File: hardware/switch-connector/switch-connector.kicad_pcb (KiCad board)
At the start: 2 copper layers, 10 parts, among them P1 12V, P2 Relay OFF (NC), P3 Sensing, P4 Coil, P5 Relay On enable (NO), P6 NO, P7 Common, SW1 NC: Off, SW2 NO: On, SW3 NC: Emergency Off

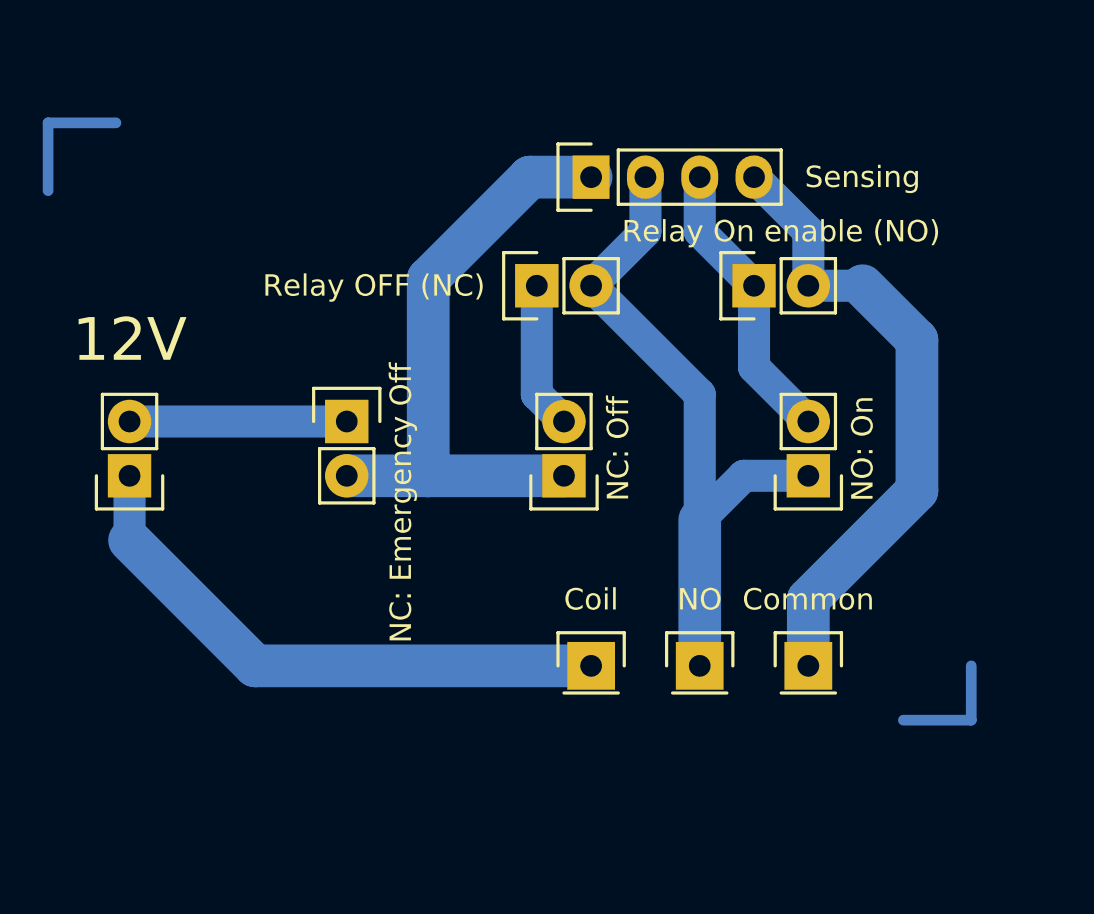
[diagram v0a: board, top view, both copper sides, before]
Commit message: o Update board with new connectors.
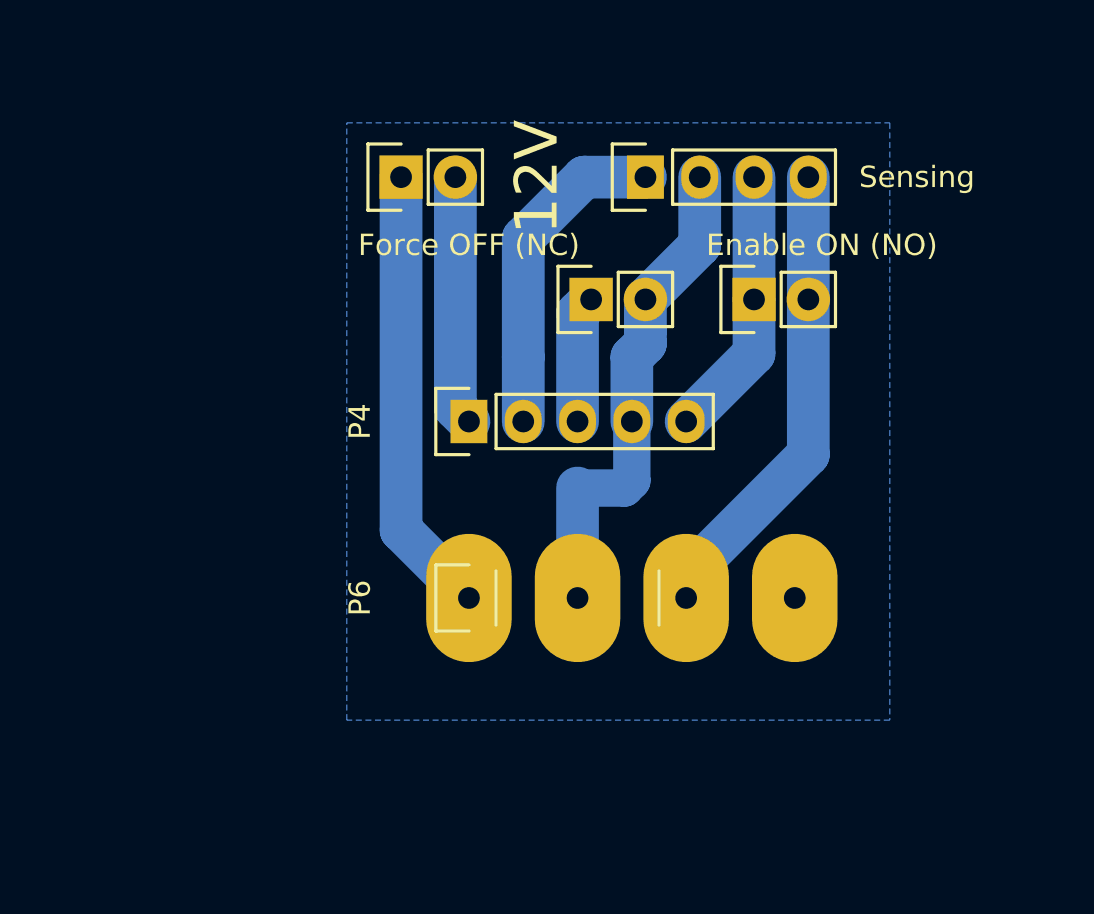
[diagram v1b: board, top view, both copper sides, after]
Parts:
- removed P7: Common, Pin_Headers:Pin_Header_Straight_1x01
- removed SW1: NC: Off, Pin_Headers:Pin_Header_Straight_1x02
- removed SW2: NO: On, Pin_Headers:Pin_Header_Straight_1x02
- removed SW3: NC: Emergency Off, Pin_Headers:Pin_Header_Straight_1x02
- P2: value Relay OFF (NC) -> Force OFF (NC)
- P4: value Coil -> SwitchConnector; footprint Pin_Headers:Pin_Header_Straight_1x01 -> Pin_Headers:Pin_Header_Straight_1x05
- P5: value Relay On enable (NO) -> Enable ON (NO)
- P6: value NO -> HV-RelayConnector; footprint Pin_Headers:Pin_Header_Straight_1x01 -> Pin_Headers:Pin_Header_Straight_1x04
- moved P1 18.9 mm to (168.9, 100.3), turned to 90 degrees
- moved P4 12.8 mm to (172.1, 111.8), turned to 90 degrees
- moved P6 11.3 mm to (172.1, 120.0), turned to 90 degrees
- moved P2 2.62 mm to (177.8, 106.0)
- moved P3 2.54 mm to (180.3, 100.3)
- moved P5 0.64 mm to (185.4, 106.0)
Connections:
- P1 pad 1: Net-(P1-Pad1) -> GND
- P1 pad 2: Net-(P1-Pad2) -> +12V
- P2 pad 2: Net-(P2-Pad2) -> /switch-box/Sense-Off
- P3 pad 1: Net-(P3-Pad1) -> /switch-box/Sense-E-Stop
- P3 pad 2: Net-(P2-Pad2) -> /switch-box/Sense-Off
- P3 pad 3: Net-(P3-Pad3) -> /switch-box/Sense-On
- P3 pad 4: Net-(P3-Pad4) -> /switch-box/Sense-Powered
- P4 pad 1: Net-(P1-Pad1) -> +12V
- P5 pad 1: Net-(P3-Pad3) -> /switch-box/Sense-On
- P5 pad 2: Net-(P3-Pad4) -> /switch-box/Sense-Powered
- P6 pad 1: Net-(P2-Pad2) -> GND
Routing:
- net Net-(P2-Pad2): track 32.0 -> 0.00 mm
- net Net-(P3-Pad4): track 29.6 -> 0.00 mm
- net Net-(P3-Pad1): track 29.0 -> 0.00 mm
- net Net-(P1-Pad1): track 27.0 -> 0.00 mm
- net /switch-box/Sense-Off: track 0.00 -> 26.1 mm
- net /switch-box/Sense-Powered: track 0.00 -> 22.1 mm
- net GND: track 0.00 -> 21.0 mm
- net /switch-box/Sense-E-Stop: track 0.00 -> 15.5 mm
- net Net-(P3-Pad3): track 13.5 -> 0.00 mm
- net /switch-box/Sense-On: track 0.00 -> 12.7 mm
- net (no net): track 12.1 -> 0.00 mm
- net +12V: track 0.00 -> 11.7 mm
- net Net-(P1-Pad2): track 10.2 -> 0.00 mm
- net Net-(P2-Pad1): track 6.88 -> 5.97 mm
- added copper zone on B.Cu, net GND
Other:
- net class Default: clearance 0.2 -> 0.25
- rule trace_clearance: 0.2 -> 0.25

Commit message: o tweaks.
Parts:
- added REF**: M, Mounting_Holes:MountingHole_3.2mm_M3, F.Cu at (194.0, 122.0)
- added REF**: M, Mounting_Holes:MountingHole_3.2mm_M3, F.Cu at (194.0, 102.0)
- added REF**: M, Mounting_Holes:MountingHole_3.2mm_M3, F.Cu at (163.0, 102.0)
- added REF**: M, Mounting_Holes:MountingHole_3.2mm_M3, F.Cu at (163.0, 122.0)
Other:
- board outline added: 40 x 27.9 mm
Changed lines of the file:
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@@
     (links 11)
     (no_connects 0)
-    (area 0 0 0 0)
+    (area 157.899999 96.7925 198.100001 125.830001)
     (thickness 1.6)
     (drawings 4)
     (tracks 28)
     (zones 0)
-    (modules 6)
+    (modules 10)
     (nets 8)
   )
@@
   )
   (setup
-    (last_trace_width 2)
+    (last_trace_width 1.5)
     (user_trace_width 1.5)
     (user_trace_width 1.75)
@@
     (trace_min 0.2)
     (segment_width 0.2)
-    (edge_width 0.15)
+    (edge_width 0.2)
     (via_size 0.6)
     (via_drill 0.4)
@@
     (mod_text_size 1 1)
     (mod_text_width 0.15)
-    (pad_size 1.524 1.524)
-    (pad_drill 0.762)
+    (pad_size 3.2 3.2)
+    (pad_drill 3.2)
     (pad_to_mask_clearance 0.2)
     (aux_axis_origin 0 0)
     (visible_elements FFFFEF7F)
     (pcbplotparams
-      (layerselection 0x00020_80000000)
+      (layerselection 0x00000_fffffffe)
       (usegerberextensions false)
       (excludeedgelayer true)
@@
     (diff_pair_width 0.2)
   )
+  (module Mounting_Holes:MountingHole_3.2mm_M3 locked (layer F.Cu)
+    (at 194 122)
+    (descr "Mounting Hole 3.2mm, no annular, M3")
+    (tags "mounting hole 3.2mm no annular m3")
+    (fp_text reference REF** (at 0 -4.2) (layer F.SilkS)
+      (effects (font (size 1 1) (thickness 0.15)))
+    )
+    (fp_text value M (at 0 0) (layer F.Fab)
+      (effects (font (size 1 1) (thickness 0.15)))
+    )
+    (fp_circle (center 0 0) (end 3.2 0) (layer Cmts.User) (width 0.15))
+    (fp_circle (center 0 0) (end 3.45 0) (layer F.CrtYd) (width 0.05))
+    (pad 1 np_thru_hole circle (at 0 0) (size 3.2 3.2) (drill 3.2) (layers *.Cu *.Mask F.SilkS))
+  )
+  (module Mounting_Holes:MountingHole_3.2mm_M3 locked (layer F.Cu)
+    (at 194 102)
+    (descr "Mounting Hole 3.2mm, no annular, M3")
+    (tags "mounting hole 3.2mm no annular m3")
+    (fp_text reference REF** (at 0 -4.2) (layer F.SilkS)
+      (effects (font (size 1 1) (thickness 0.15)))
+    )
+    (fp_text value M (at 0 0 180) (layer F.Fab)
+      (effects (font (size 1 1) (thickness 0.15)))
+    )
+    (fp_circle (center 0 0) (end 3.45 0) (layer F.CrtYd) (width 0.05))
+    (fp_circle (center 0 0) (end 3.2 0) (layer Cmts.User) (width 0.15))
+    (pad 1 np_thru_hole circle (at 0 0) (size 3.2 3.2) (drill 3.2) (layers *.Cu *.Mask F.SilkS))
+  )
+  (module Mounting_Holes:MountingHole_3.2mm_M3 locked (layer F.Cu)
+    (at 163 102)
+    (descr "Mounting Hole 3.2mm, no annular, M3")
+    (tags "mounting hole 3.2mm no annular m3")
+    (fp_text reference REF** (at 0 -4.2) (layer F.SilkS)
+      (effects (font (size 1 1) (thickness 0.15)))
+    )
+    (fp_text value M (at 0 0) (layer F.Fab)
+      (effects (font (size 1 1) (thickness 0.15)))
+    )
+    (fp_circle (center 0 0) (end 3.2 0) (layer Cmts.User) (width 0.15))
+    (fp_circle (center 0 0) (end 3.45 0) (layer F.CrtYd) (width 0.05))
+    (pad 1 np_thru_hole circle (at 0 0) (size 3.2 3.2) (drill 3.2) (layers *.Cu *.Mask F.SilkS))
+  )
+  (module Mounting_Holes:MountingHole_3.2mm_M3 locked (layer F.Cu)
+    (at 163 122)
+    (descr "Mounting Hole 3.2mm, no annular, M3")
+    (tags "mounting hole 3.2mm no annular m3")
+    (fp_text reference REF** (at 0 -4.2) (layer F.SilkS)
+      (effects (font (size 1 1) (thickness 0.15)))
+    )
+    (fp_text value M (at 0 0) (layer F.Fab)
+      (effects (font (size 1 1) (thickness 0.15)))
+    )
+    (fp_circle (center 0 0) (end 3.45 0) (layer F.CrtYd) (width 0.05))
+    (fp_circle (center 0 0) (end 3.2 0) (layer Cmts.User) (width 0.15))
+    (pad 1 np_thru_hole circle (at 0 0) (size 3.2 3.2) (drill 3.2) (layers *.Cu *.Mask F.SilkS))
+  )
   (module Pin_Headers:Pin_Header_Straight_1x04 (layer F.Cu)
     (at 172.085 120.015 90)
@@
     )
   )
-  (gr_line (start 166.37 125.73) (end 166.37 97.79) (layer Margin) (width 0.2))
-  (gr_line (start 191.77 125.73) (end 166.37 125.73) (layer Margin) (width 0.2))
-  (gr_line (start 191.77 97.79) (end 191.77 125.73) (layer Margin) (width 0.2))
-  (gr_line (start 166.37 97.79) (end 191.77 97.79) (layer Margin) (width 0.2))
+  (gr_line (start 158 125.73) (end 158 97.79) (layer Edge.Cuts) (width 0.2))
+  (gr_line (start 198 125.73) (end 158 125.73) (layer Edge.Cuts) (width 0.2))
+  (gr_line (start 198 97.79) (end 198 125.73) (layer Edge.Cuts) (width 0.2))
+  (gr_line (start 158 97.79) (end 198 97.79) (layer Edge.Cuts) (width 0.2))
   (segment (start 177.8 106.05) (end 177.165 106.685) (width 2) (layer B.Cu) (net 1))
   (segment (start 177.165 106.685) (end 177.165 111.76) (width 2) (layer B.Cu) (net 1))
@@
     (polygon
       (pts
-        (xy 166.37 97.79) (xy 191.77 97.79) (xy 191.77 125.73) (xy 166.37 125.73)
+        (xy 158.75 97.79) (xy 197.485 97.79) (xy 197.485 125.73) (xy 158.75 125.73)
       )
     )

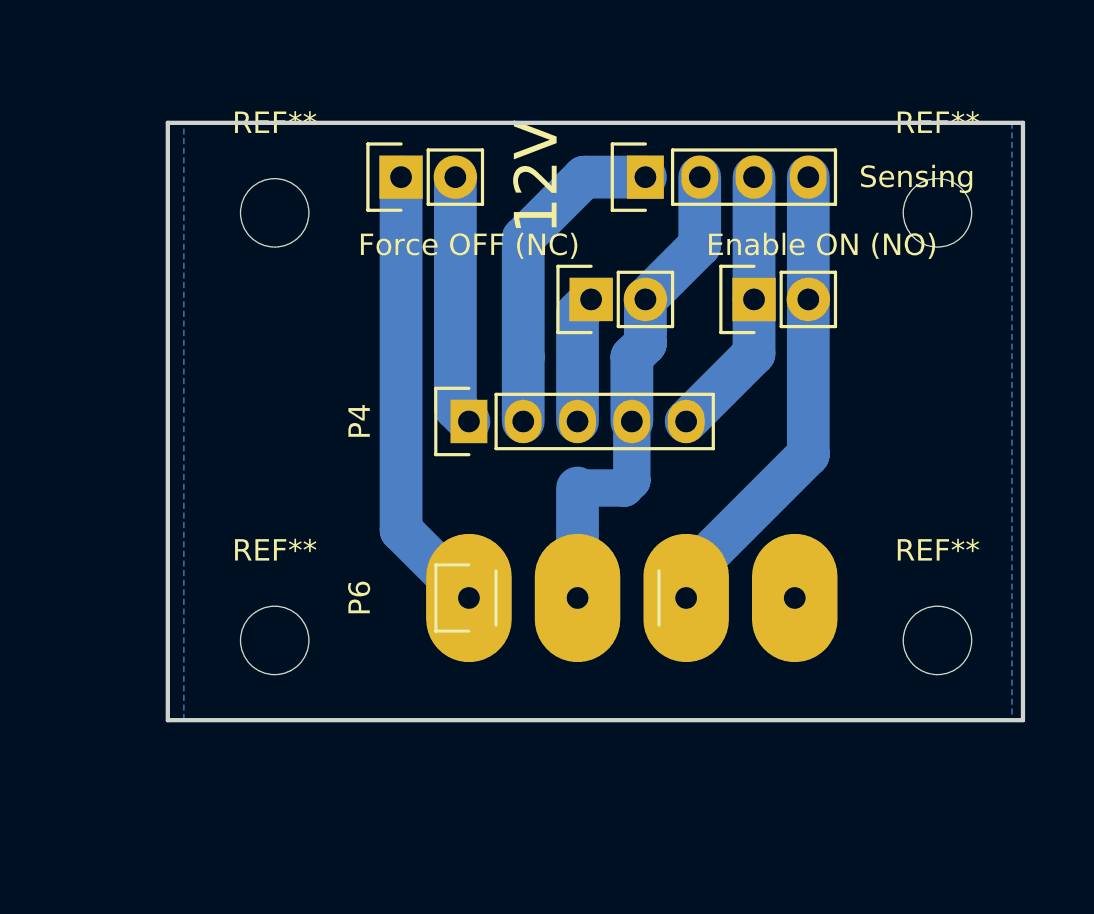
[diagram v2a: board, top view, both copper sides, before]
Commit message: A little more silkscreen to ease assembly.
Also:
o enough space for actual connectors for switches and sense outputs
o have inputs for every single switch ('eStop' and 'off' were sharing one)
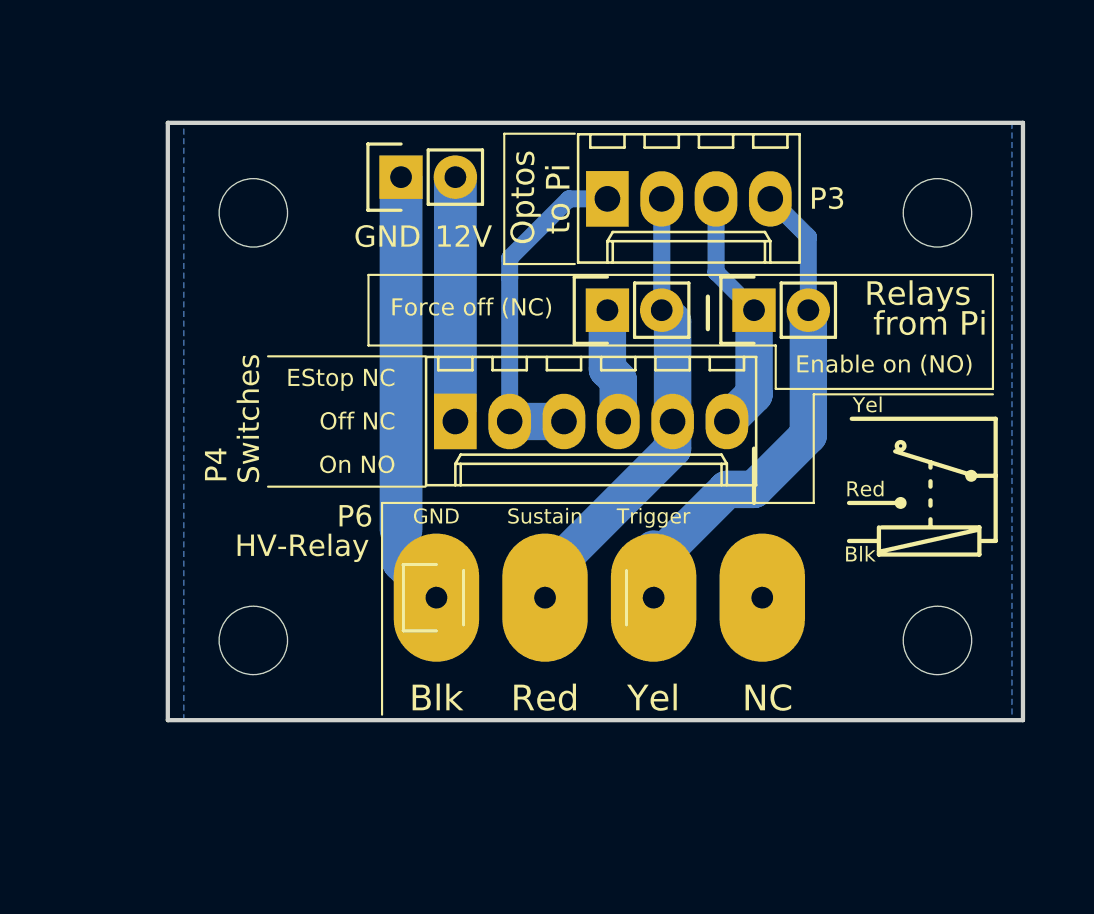
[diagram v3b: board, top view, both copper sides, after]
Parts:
- P2: value Force OFF (NC) -> Force off (NC)
- P3: value Sensing -> 12V Sensing; footprint Pin_Headers:Pin_Header_Straight_1x04 -> Connectors_Molex:Molex_KK-6410-04_04x2.54mm_Straight
- P4: value SwitchConnector -> Switches; footprint Pin_Headers:Pin_Header_Straight_1x05 -> Connectors_Molex:Molex_KK-6410-06_06x2.54mm_Straight
- P5: value Enable ON (NO) -> Enable on (NO)
- P6: value HV-RelayConnector -> HV-Relay
- moved P3 2.05 mm to (178.6, 101.3), turned to 0 degrees
- moved P6 1.52 mm to (170.6, 120.0)
- moved REF** 1.00 mm to (162.0, 102.0)
- moved REF** 1.00 mm to (162.0, 122.0)
- moved P2 0.91 mm to (178.6, 106.6)
- moved P4 0.64 mm to (171.4, 111.8), turned to 0 degrees
- moved P5 0.50 mm to (185.4, 106.6)
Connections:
- net /switch-box/Sense-Powered renamed /Trigger
- P2 pad 2: /switch-box/Sense-Off -> /Sustain
- P3 pad 2: /switch-box/Sense-Off -> /Sustain
- P4 pad 3: Net-(P2-Pad1) -> /switch-box/Sense-E-Stop
- P4 pad 4: /switch-box/Sense-Off -> Net-(P2-Pad1)
- P4 pad 5: /switch-box/Sense-On -> /Sustain
- P6 pad 2: /switch-box/Sense-Off -> /Sustain
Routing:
- net /switch-box/Sense-Off: track 26.1 -> 0.00 mm
- net /Sustain: track 0.00 -> 23.8 mm
- net /Trigger: track 22.1 -> 30.4 mm
- net /switch-box/Sense-On: track 12.7 -> 11.7 mm
- net +12V: track 11.7 -> 10.8 mm
- net GND: track 21.0 -> 20.4 mm
- net Net-(P2-Pad1): track 5.97 -> 5.42 mm
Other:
- board text added: "Blk"
- board text added: "EStop NC"
- board text added: "GND"
- board text added: "NC"
- board text added: "Off NC"
- board text added: "On NO"
- board text added: "Optos"
- board text added: "Red"
- board text added: "Relays"
- board text added: "Sustain"
- board text added: "Trigger"
- board text added: "Yel"
- board text added: "from Pi"
- board text added: "to Pi"
